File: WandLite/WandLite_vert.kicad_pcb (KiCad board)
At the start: 2 copper layers, 12.1 x 25.6 mm, 7 parts, among them U1 ATtiny85-20P

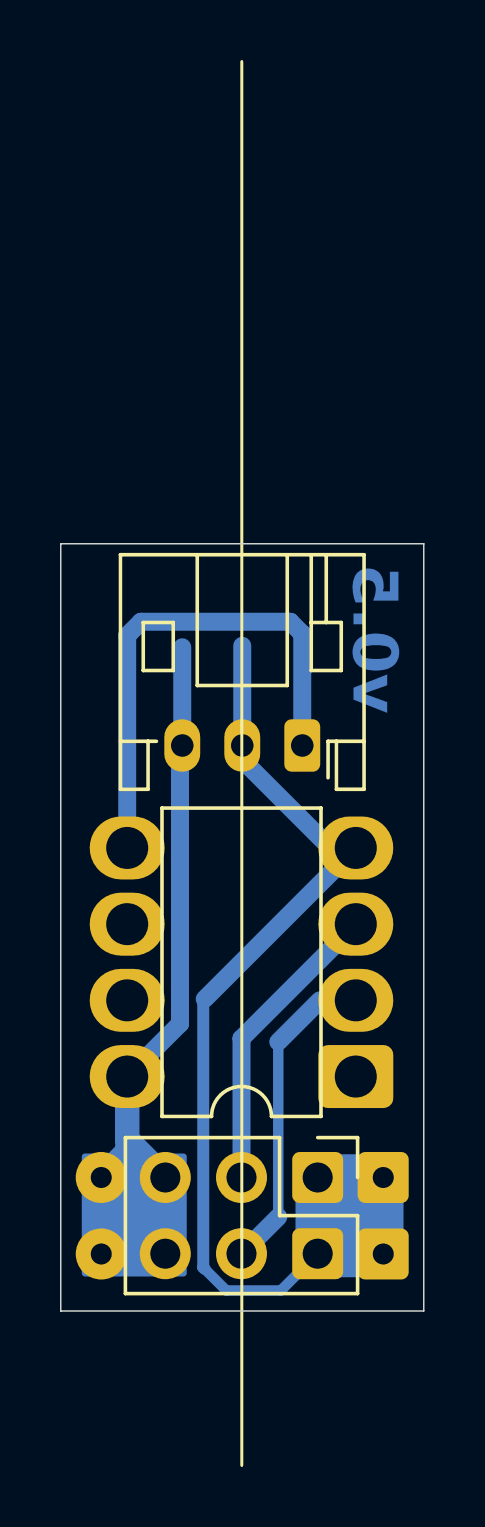
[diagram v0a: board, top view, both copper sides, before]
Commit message: v5 made vertical
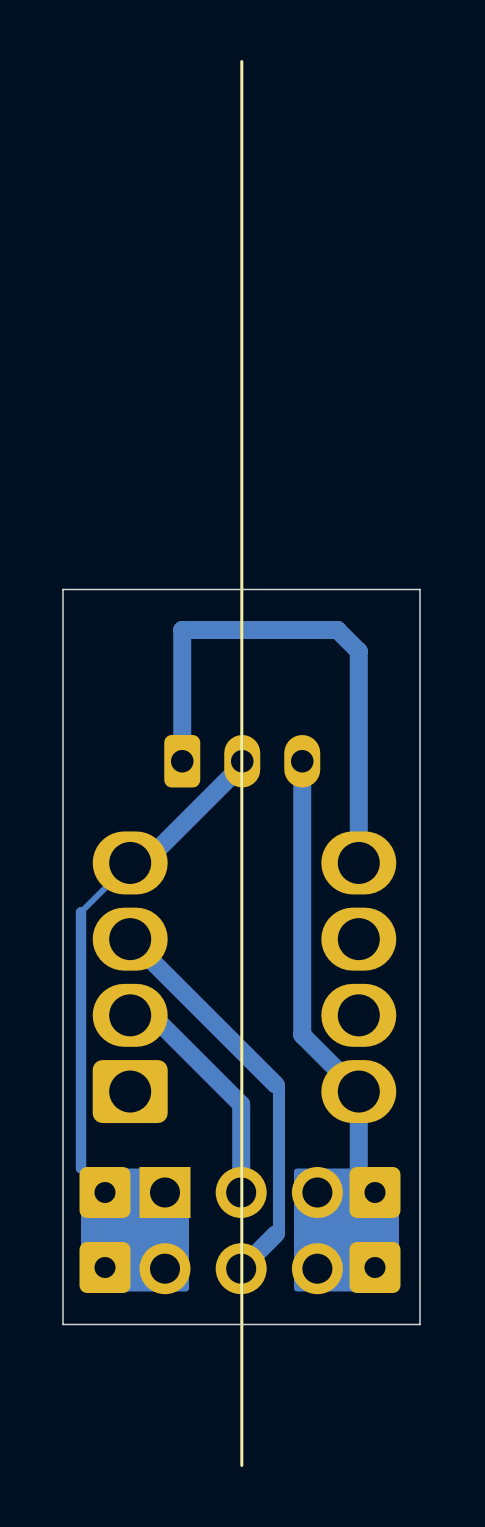
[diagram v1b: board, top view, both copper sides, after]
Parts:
- BLD-O1, GND-I1, GND-I2, J-IN1, U1: moved to B.Cu
- moved ? 9.61 mm to (170.6, 131.4)
- moved VCC-I1 9.35 mm to (170.6, 128.9)
- moved GND-I2 9.29 mm to (161.6, 128.9), turned to 0 degrees
- moved GND-I1 9.29 mm to (161.6, 131.4), turned to 0 degrees
- moved U1 7.54 mm to (162.4, 125.5), turned to 0 degrees
- moved J-IN1 5.11 mm to (163.6, 128.9)
- moved BLD-O1 4.03 mm to (164.2, 114.5), turned to 0 degrees
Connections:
- U1 pad 2: Net-(J-IN1-Pin_4) -> Net-(J-IN1-Pin_3)
- U1 pad 3: Net-(J-IN1-Pin_3) -> Net-(J-IN1-Pin_4)
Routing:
- net GND: track 32.1 -> 26.3 mm
- net Net-(J-IN1-Pin_4): track 10.7 -> 13.5 mm
- net VCC: track 27.4 -> 25.2 mm
- net Net-(J-IN1-Pin_3): track 10.0 -> 7.87 mm
- net Net-(BLD-O1-Pin_1): track 17.0 -> 17.6 mm
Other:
- board size 12.1 x 25.6 mm -> 11.9 x 24.5 mm
- board text removed: "v0.5"
